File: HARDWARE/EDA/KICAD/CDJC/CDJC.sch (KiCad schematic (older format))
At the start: 63 parts, among them J1 COM_IN, J2 COM_OUT, J3 POWER_IN, J4 POWER_OUT, J5 BIT_OUT, Q1 BC549, SW1 B-SET, U1 74LS04, U2 74LS32, U3 74LS08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

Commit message: adjust layout pcb
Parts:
- Q1: footprint Package_TO_SOT_THT:TO-92_Inline -> Resistor_THT:R_Axial_DIN0207_L6.3mm_D2.5mm_P2.54mm_Vertical
- R1, R10, R11, R12, R13, R14, R17, R2, R3, R4, R5, R6, R7, R8, R9: footprint Resistor_THT:R_Axial_DIN0207_L6.3mm_D2.5mm_P7.62mm_Horizontal -> Resistor_THT:R_Axial_DIN0207_L6.3mm_D2.5mm_P2.54mm_Vertical
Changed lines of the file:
@@
 F 0 "R1" V 1600 1400 50  0000 L CNN
 F 1 "300K" V 1600 1150 50  0000 L CNN
-F 2 "Resistor_THT:R_Axial_DIN0207_L6.3mm_D2.5mm_P7.62mm_Horizontal" V 1430 1350 50  0001 C CNN
+F 2 "Resistor_THT:R_Axial_DIN0207_L6.3mm_D2.5mm_P2.54mm_Vertical" V 1430 1350 50  0001 C CNN
 F 3 "~" H 1500 1350 50  0001 C CNN
 	1    1500 1350
@@
 F 0 "R2" V 1800 1400 50  0000 L CNN
 F 1 "300K" V 1800 1150 50  0000 L CNN
-F 2 "Resistor_THT:R_Axial_DIN0207_L6.3mm_D2.5mm_P7.62mm_Horizontal" V 1630 1350 50  0001 C CNN
+F 2 "Resistor_THT:R_Axial_DIN0207_L6.3mm_D2.5mm_P2.54mm_Vertical" V 1630 1350 50  0001 C CNN
 F 3 "~" H 1700 1350 50  0001 C CNN
 	1    1700 1350
@@
 F 0 "R3" V 2000 1400 50  0000 L CNN
 F 1 "300K" V 2000 1150 50  0000 L CNN
-F 2 "Resistor_THT:R_Axial_DIN0207_L6.3mm_D2.5mm_P7.62mm_Horizontal" V 1830 1350 50  0001 C CNN
+F 2 "Resistor_THT:R_Axial_DIN0207_L6.3mm_D2.5mm_P2.54mm_Vertical" V 1830 1350 50  0001 C CNN
 F 3 "~" H 1900 1350 50  0001 C CNN
 	1    1900 1350
@@
 F 0 "R4" V 2250 1400 50  0000 L CNN
 F 1 "150K" V 2250 1150 50  0000 L CNN
-F 2 "Resistor_THT:R_Axial_DIN0207_L6.3mm_D2.5mm_P7.62mm_Horizontal" V 2080 1350 50  0001 C CNN
+F 2 "Resistor_THT:R_Axial_DIN0207_L6.3mm_D2.5mm_P2.54mm_Vertical" V 2080 1350 50  0001 C CNN
 F 3 "~" H 2150 1350 50  0001 C CNN
 	1    2150 1350
@@
 F 0 "R5" V 2450 1400 50  0000 L CNN
 F 1 "150K" V 2450 1150 50  0000 L CNN
-F 2 "Resistor_THT:R_Axial_DIN0207_L6.3mm_D2.5mm_P7.62mm_Horizontal" V 2280 1350 50  0001 C CNN
+F 2 "Resistor_THT:R_Axial_DIN0207_L6.3mm_D2.5mm_P2.54mm_Vertical" V 2280 1350 50  0001 C CNN
 F 3 "~" H 2350 1350 50  0001 C CNN
 	1    2350 1350
@@
 F 0 "R6" V 2650 1400 50  0000 L CNN
 F 1 "150K" V 2650 1150 50  0000 L CNN
-F 2 "Resistor_THT:R_Axial_DIN0207_L6.3mm_D2.5mm_P7.62mm_Horizontal" V 2480 1350 50  0001 C CNN
+F 2 "Resistor_THT:R_Axial_DIN0207_L6.3mm_D2.5mm_P2.54mm_Vertical" V 2480 1350 50  0001 C CNN
 F 3 "~" H 2550 1350 50  0001 C CNN
 	1    2550 1350
@@
 F 0 "R7" V 3400 1400 50  0000 L CNN
 F 1 "150K" V 3400 1150 50  0000 L CNN
-F 2 "Resistor_THT:R_Axial_DIN0207_L6.3mm_D2.5mm_P7.62mm_Horizontal" V 3230 1350 50  0001 C CNN
+F 2 "Resistor_THT:R_Axial_DIN0207_L6.3mm_D2.5mm_P2.54mm_Vertical" V 3230 1350 50  0001 C CNN
 F 3 "~" H 3300 1350 50  0001 C CNN
 	1    3300 1350
@@
 F 0 "R10" V 3700 1400 50  0000 L CNN
 F 1 "150K" V 3700 1150 50  0000 L CNN
-F 2 "Resistor_THT:R_Axial_DIN0207_L6.3mm_D2.5mm_P7.62mm_Horizontal" V 3530 1350 50  0001 C CNN
+F 2 "Resistor_THT:R_Axial_DIN0207_L6.3mm_D2.5mm_P2.54mm_Vertical" V 3530 1350 50  0001 C CNN
 F 3 "~" H 3600 1350 50  0001 C CNN
 	1    3600 1350
@@
 F 0 "R12" V 4000 1400 50  0000 L CNN
 F 1 "150K" V 4000 1150 50  0000 L CNN
-F 2 "Resistor_THT:R_Axial_DIN0207_L6.3mm_D2.5mm_P7.62mm_Horizontal" V 3830 1350 50  0001 C CNN
+F 2 "Resistor_THT:R_Axial_DIN0207_L6.3mm_D2.5mm_P2.54mm_Vertical" V 3830 1350 50  0001 C CNN
 F 3 "~" H 3900 1350 50  0001 C CNN
 	1    3900 1350
@@
 F 0 "R13" V 4400 1400 50  0000 L CNN
 F 1 "150K" V 4400 1150 50  0000 L CNN
-F 2 "Resistor_THT:R_Axial_DIN0207_L6.3mm_D2.5mm_P7.62mm_Horizontal" V 4230 1350 50  0001 C CNN
+F 2 "Resistor_THT:R_Axial_DIN0207_L6.3mm_D2.5mm_P2.54mm_Vertical" V 4230 1350 50  0001 C CNN
 F 3 "~" H 4300 1350 50  0001 C CNN
 	1    4300 1350
@@
 F 0 "R14" V 4700 1400 50  0000 L CNN
 F 1 "150K" V 4700 1150 50  0000 L CNN
-F 2 "Resistor_THT:R_Axial_DIN0207_L6.3mm_D2.5mm_P7.62mm_Horizontal" V 4530 1350 50  0001 C CNN
+F 2 "Resistor_THT:R_Axial_DIN0207_L6.3mm_D2.5mm_P2.54mm_Vertical" V 4530 1350 50  0001 C CNN
 F 3 "~" H 4600 1350 50  0001 C CNN
 	1    4600 1350
@@
 F 0 "R8" V 3450 7250 50  0000 L CNN
 F 1 "300K" V 3450 7000 50  0000 L CNN
-F 2 "Resistor_THT:R_Axial_DIN0207_L6.3mm_D2.5mm_P7.62mm_Horizontal" V 3280 7200 50  0001 C CNN
+F 2 "Resistor_THT:R_Axial_DIN0207_L6.3mm_D2.5mm_P2.54mm_Vertical" V 3280 7200 50  0001 C CNN
 F 3 "~" H 3350 7200 50  0001 C CNN
 	1    3350 7200
@@
 F 0 "R9" V 3650 7250 50  0000 L CNN
 F 1 "300K" V 3650 7000 50  0000 L CNN
-F 2 "Resistor_THT:R_Axial_DIN0207_L6.3mm_D2.5mm_P7.62mm_Horizontal" V 3480 7200 50  0001 C CNN
+F 2 "Resistor_THT:R_Axial_DIN0207_L6.3mm_D2.5mm_P2.54mm_Vertical" V 3480 7200 50  0001 C CNN
 F 3 "~" H 3550 7200 50  0001 C CNN
 	1    3550 7200
@@
 F 0 "R11" V 3850 7250 50  0000 L CNN
 F 1 "300K" V 3850 7000 50  0000 L CNN
-F 2 "Resistor_THT:R_Axial_DIN0207_L6.3mm_D2.5mm_P7.62mm_Horizontal" V 3680 7200 50  0001 C CNN
+F 2 "Resistor_THT:R_Axial_DIN0207_L6.3mm_D2.5mm_P2.54mm_Vertical" V 3680 7200 50  0001 C CNN
 F 3 "~" H 3750 7200 50  0001 C CNN
 	1    3750 7200
@@
 F 0 "R17" V 9050 4750 50  0000 L CNN
 F 1 "300K" V 8850 4750 50  0000 L CNN
-F 2 "Resistor_THT:R_Axial_DIN0207_L6.3mm_D2.5mm_P7.62mm_Horizontal" V 8880 4850 50  0001 C CNN
+F 2 "Resistor_THT:R_Axial_DIN0207_L6.3mm_D2.5mm_P2.54mm_Vertical" V 8880 4850 50  0001 C CNN
 F 3 "~" H 8950 4850 50  0001 C CNN
 	1    8950 4850
@@
 F 0 "Q1" H 9041 5346 50  0000 L CNN
 F 1 "BC549" H 9041 5255 50  0000 L CNN
-F 2 "Package_TO_SOT_THT:TO-92_Inline" H 9050 5225 50  0001 L CIN
+F 2 "Resistor_THT:R_Axial_DIN0207_L6.3mm_D2.5mm_P2.54mm_Vertical" H 9050 5225 50  0001 L CIN
 F 3 "http://www.fairchildsemi.com/ds/BC/BC547.pdf" H 8850 5300 50  0001 L CNN
 	1    8850 5300

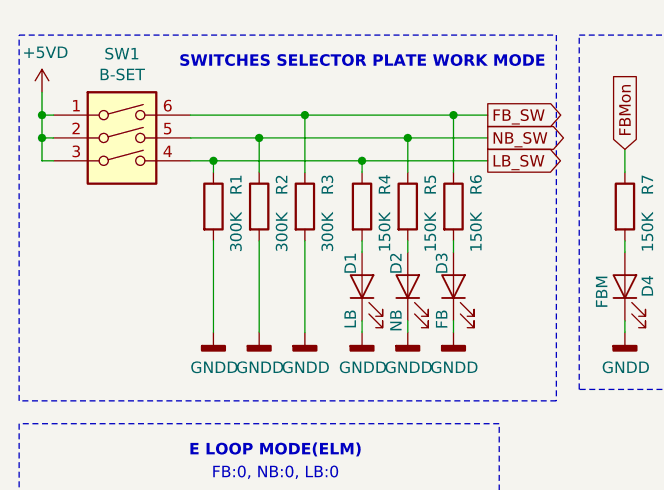
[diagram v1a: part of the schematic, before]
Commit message: ajust dip and leds mode set
adjust jumper to set mode
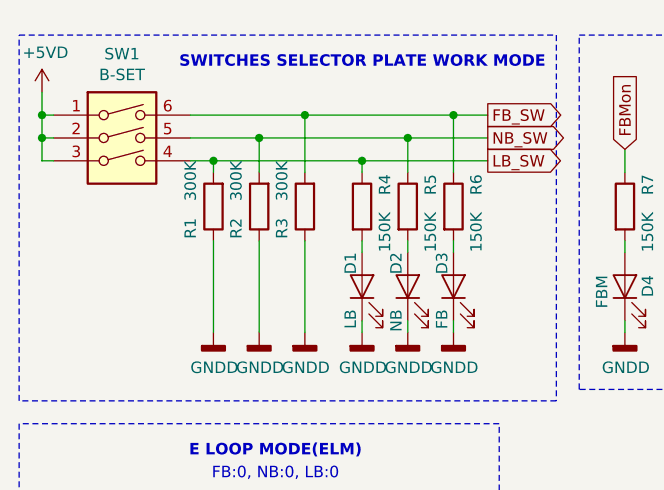
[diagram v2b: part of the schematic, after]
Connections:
- net FB_SW: now also R3.2; no longer R3.1
- net GNDD: now also R1.1, R2.1, R3.1; no longer R1.2, R2.2, R3.2
- net LB_SW: now also R1.2; no longer R1.1
- net NB_SW: now also R2.2; no longer R2.1
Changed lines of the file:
@@
 F 3 "~" H 1500 1350 50  0001 C CNN
 	1    1500 1350
-	1    0    0    -1
+	-1   0    0    1
 $EndComp
 $Comp
@@
 F 3 "~" H 1700 1350 50  0001 C CNN
 	1    1700 1350
-	1    0    0    -1
+	-1   0    0    1
 $EndComp
 $Comp
@@
 F 3 "~" H 1900 1350 50  0001 C CNN
 	1    1900 1350
-	1    0    0    -1
+	-1   0    0    1
 $EndComp
 Wire Wire Line

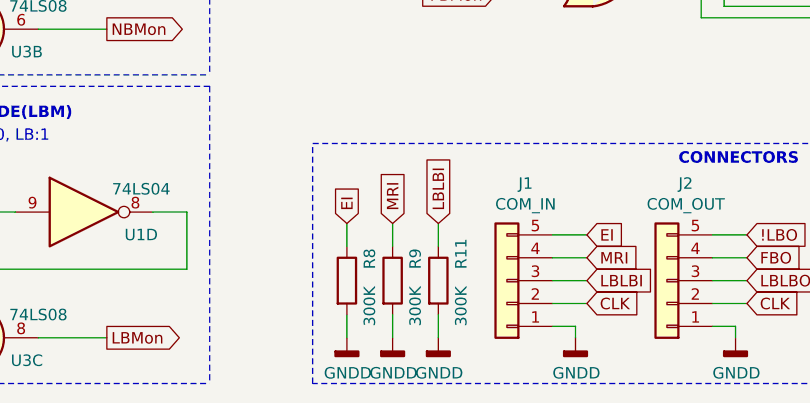
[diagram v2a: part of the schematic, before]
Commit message: adjust footprint to bc 547
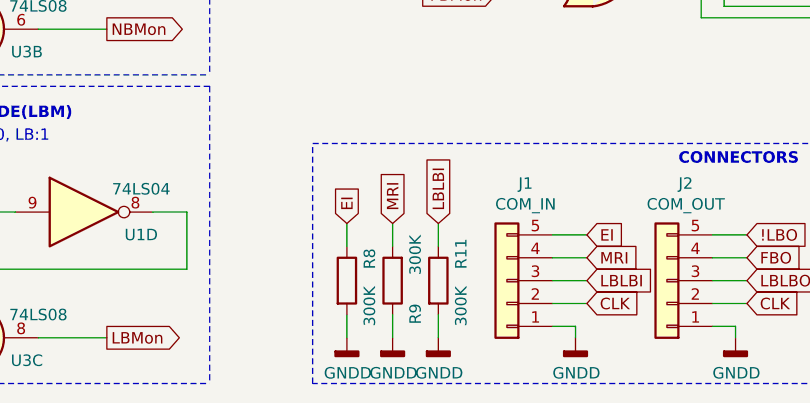
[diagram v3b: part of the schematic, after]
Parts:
- Q1: footprint Resistor_THT:R_Axial_DIN0207_L6.3mm_D2.5mm_P2.54mm_Vertical -> Package_TO_SOT_THT:TO-92_Inline
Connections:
- net GNDD: now also R9.1; no longer R9.2
- net MRI: now also R9.2; no longer R9.1
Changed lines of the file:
@@
 U 1 1 62F38E35
 P 3550 7200
-F 0 "R9" V 3650 7250 50  0000 L CNN
-F 1 "300K" V 3650 7000 50  0000 L CNN
+F 0 "R9" V 3450 7300 50  0000 L CNN
+F 1 "300K" V 3450 7000 50  0000 L CNN
 F 2 "Resistor_THT:R_Axial_DIN0207_L6.3mm_D2.5mm_P2.54mm_Vertical" V 3480 7200 50  0001 C CNN
 F 3 "~" H 3550 7200 50  0001 C CNN
 	1    3550 7200
-	1    0    0    -1
+	-1   0    0    1
 $EndComp
 Wire Wire Line
@@
 F 0 "Q1" H 9041 5346 50  0000 L CNN
 F 1 "BC549" H 9041 5255 50  0000 L CNN
-F 2 "Resistor_THT:R_Axial_DIN0207_L6.3mm_D2.5mm_P2.54mm_Vertical" H 9050 5225 50  0001 L CIN
+F 2 "Package_TO_SOT_THT:TO-92_Inline" H 9050 5225 50  0001 L CIN
 F 3 "http://www.fairchildsemi.com/ds/BC/BC547.pdf" H 8850 5300 50  0001 L CNN
 	1    8850 5300

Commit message: stop work, go home
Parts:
- D20, D21, D9: footprint Diode_THT:D_DO-34_SOD68_P7.62mm_Horizontal -> Diode_THT:D_DO-34_SOD68_P2.54mm_Vertical_AnodeUp
- R15, R16: footprint Resistor_THT:R_Axial_DIN0207_L6.3mm_D2.5mm_P7.62mm_Horizontal -> Resistor_THT:R_Axial_DIN0207_L6.3mm_D2.5mm_P2.54mm_Vertical
- R17: footprint Resistor_THT:R_Axial_DIN0207_L6.3mm_D2.5mm_P2.54mm_Vertical -> Resistor_THT:R_Axial_DIN0207_L6.3mm_D2.5mm_P7.62mm_Horizontal
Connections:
- net GNDD: now also R9.2; no longer R9.1
- net MRI: now also R9.1, U6.4; no longer R9.2, U6.5
- net MRLMon: now also U6.13; no longer U6.12
- net at U6.2, U8.8: now also U6.5; no longer U6.4
- net at D10.1 (K), R16.2, U5.12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: now also U6.12; no longer U6.13
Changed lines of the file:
@@
 U 1 1 62F38E35
 P 3550 7200
-F 0 "R9" V 3450 7300 50  0000 L CNN
-F 1 "300K" V 3450 7000 50  0000 L CNN
+F 0 "R9" V 3650 7250 50  0000 L CNN
+F 1 "300K" V 3650 7000 50  0000 L CNN
 F 2 "Resistor_THT:R_Axial_DIN0207_L6.3mm_D2.5mm_P2.54mm_Vertical" V 3480 7200 50  0001 C CNN
 F 3 "~" H 3550 7200 50  0001 C CNN
 	1    3550 7200
-	-1   0    0    1
+	1    0    0    -1
 $EndComp
 Wire Wire Line
@@
 F 0 "R17" V 9050 4750 50  0000 L CNN
 F 1 "300K" V 8850 4750 50  0000 L CNN
-F 2 "Resistor_THT:R_Axial_DIN0207_L6.3mm_D2.5mm_P2.54mm_Vertical" V 8880 4850 50  0001 C CNN
+F 2 "Resistor_THT:R_Axial_DIN0207_L6.3mm_D2.5mm_P7.62mm_Horizontal" V 8880 4850 50  0001 C CNN
 F 3 "~" H 8950 4850 50  0001 C CNN
 	1    8950 4850
@@
 F 0 "R15" V 8700 5450 50  0000 L CNN
 F 1 "150K" V 8500 5350 50  0000 L CNN
-F 2 "Resistor_THT:R_Axial_DIN0207_L6.3mm_D2.5mm_P7.62mm_Horizontal" V 8530 5450 50  0001 C CNN
+F 2 "Resistor_THT:R_Axial_DIN0207_L6.3mm_D2.5mm_P2.54mm_Vertical" V 8530 5450 50  0001 C CNN
 F 3 "~" H 8600 5450 50  0001 C CNN
 	1    8600 5450
@@
 F 0 "R16" V 8450 5300 50  0000 L CNN
 F 1 "1K" V 8450 5150 50  0000 L CNN
-F 2 "Resistor_THT:R_Axial_DIN0207_L6.3mm_D2.5mm_P7.62mm_Horizontal" V 8280 5300 50  0001 C CNN
+F 2 "Resistor_THT:R_Axial_DIN0207_L6.3mm_D2.5mm_P2.54mm_Vertical" V 8280 5300 50  0001 C CNN
 F 3 "~" H 8350 5300 50  0001 C CNN
 	1    8350 5300
@@
 U 4 1 625ABD98
 P 5950 5750
-F 0 "U6" H 6200 5700 50  0000 C CNN
-F 1 "74LS08" H 5950 5950 50  0000 C CNN
+F 0 "U6" H 6200 5800 50  0000 C CNN
+F 1 "74LS08" H 6200 5600 50  0000 C CNN
 F 2 "Package_DIP:DIP-14_W7.62mm_LongPads" H 5950 5750 50  0001 C CNN
 F 3 "http://www.ti.com/lit/gpn/sn74LS08" H 5950 5750 50  0001 C CNN
 	4    5950 5750
-	1    0    0    -1
+	1    0    0    1
 $EndComp
 $Comp
@@
 F 3 "http://www.ti.com/lit/gpn/sn74LS08" H 4400 4650 50  0001 C CNN
 	2    4400 4650
-	1    0    0    -1
+	1    0    0    1
 $EndComp
 $Comp
@@
 F 0 "D20" H 10400 4234 50  0000 C CNN
 F 1 "1N4148" H 10400 4325 50  0000 C CNN
-F 2 "Diode_THT:D_DO-34_SOD68_P7.62mm_Horizontal" H 10400 4275 50  0001 C CNN
+F 2 "Diode_THT:D_DO-34_SOD68_P2.54mm_Vertical_AnodeUp" H 10400 4275 50  0001 C CNN
 F 3 "https://assets.nexperia.com/documents/data-sheet/1N4148_1N4448.pdf" H 10400 4450 50  0001 C CNN
 	1    10400 4450
@@
 F 0 "D9" H 9750 5734 50  0000 C CNN
 F 1 "1N4148" H 9750 5825 50  0000 C CNN
-F 2 "Diode_THT:D_DO-34_SOD68_P7.62mm_Horizontal" H 9750 5775 50  0001 C CNN
+F 2 "Diode_THT:D_DO-34_SOD68_P2.54mm_Vertical_AnodeUp" H 9750 5775 50  0001 C CNN
 F 3 "https://assets.nexperia.com/documents/data-sheet/1N4148_1N4448.pdf" H 9750 5950 50  0001 C CNN
 	1    9750 5950
@@
 F 0 "D21" H 8000 4300 50  0000 C CNN
 F 1 "1N4148" H 7550 4300 50  0000 C CNN
-F 2 "Diode_THT:D_DO-34_SOD68_P7.62mm_Horizontal" H 7750 4175 50  0001 C CNN
+F 2 "Diode_THT:D_DO-34_SOD68_P2.54mm_Vertical_AnodeUp" H 7750 4175 50  0001 C CNN
 F 3 "https://assets.nexperia.com/documents/data-sheet/1N4148_1N4448.pdf" H 7750 4350 50  0001 C CNN
 	1    7750 4350

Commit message: pause work for sleep
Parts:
- removed C2, C3, C4, C5, C6, C7, C8, C9: 100nF 63V, Capacitor_THT:C_Rect_L7.0mm_W2.5mm_P5.00mm, symbol Device:C
- R11, R8, R9: footprint Resistor_THT:R_Axial_DIN0207_L6.3mm_D2.5mm_P2.54mm_Vertical -> Resistor_THT:R_Axial_DIN0207_L6.3mm_D2.5mm_P7.62mm_Horizontal
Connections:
- net !LBO: now also J2.4 (Pin_4); no longer J2.5 (Pin_5)
- net CLK: now also J1.5 (Pin_5), J2.5 (Pin_5); no longer J1.2 (Pin_2), J2.2 (Pin_2)
- net EI: now also J1.4 (Pin_4), U6.5; no longer J1.5 (Pin_5), U6.1
- net ELMon: now also U4.8; no longer U4.6
- net FBMon: now also U3.8, U6.13; no longer U3.3, U6.10
- net FBO: now also J2.3 (Pin_3); no longer J2.4 (Pin_4)
- net FB_SW: now also U1.11, U3.10, U4.1; no longer U1.1, U3.2, U4.9
- net GNDD: now also U3.1, U3.2; no longer U3.12, U3.13
- net LBLBI: now also J1.2 (Pin_2), U6.12; no longer J1.3 (Pin_3), U6.9
- net LBLBO: now also J2.2 (Pin_2); no longer J2.3 (Pin_3)
- net LBMon: now also U3.11, U8.2; no longer U3.8, U8.10
- net LB_SW: now also U1.9, U3.12; no longer U1.5, U3.10
- net MRI: now also J1.3 (Pin_3), U6.10; no longer J1.4 (Pin_4), U6.4
- net MRLMon: now also U6.2; no longer U6.13
- net NBMon: now also U8.1; no longer U8.9
- net NB_SW: now also U1.13, U4.2; no longer U1.3, U4.10
- net at U4.12: now also U4.3; no longer U4.8
- net at U2.6: now also U1.3; no longer U1.13
- net at U1.10: now also U4.5; no longer U3.4
- net at U2.8: now also U1.5; no longer U1.11
- net at U1.12: now also U4.4; no longer U3.1
- net at U1.8: now also U4.10; no longer U3.9
- net at U1.2: now also U3.13; no longer U4.1
- net at U1.4: now also U3.9; no longer U4.2
- net at U1.6: now also U3.4; no longer U4.5
- net at U2.11: now also U1.1; no longer U1.9
- net at U9.13 (CKEN): now also U8.6; no longer U8.3
- net at U9.15 (Reset): now also U8.11; no longer U8.6
- net at D10.1 (K), R16.2, U5.12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: now also U6.1; no longer U6.12
- net at U8.12: now also U8.8; no longer U6.6
- net at U5.3: now also U8.5; no longer U8.2
- net at U6.3: now also U8.13; no longer U8.1
- net at U8.4: now also U6.6; no longer U8.11
- net at U6.11: now also U8.9; no longer U8.5
- net at U6.8: now also U8.10; no longer U8.13
- new net: U4.6, U4.9
- new net: U6.4, U6.9, U8.3
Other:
- moved on the sheet: U1A, U1B, U1C, U1D, U1E, U1F, U3A, U3C, U3D, U4A, U4B, U4C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
